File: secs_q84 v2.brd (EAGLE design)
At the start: 97.5 x 69.8 mm, 122 parts, among them IC1 MAX203ECWP, IC2 REF3440TIDBVR, IC3 ADP151AUJZ-3.3-R7, IC4 ADM3095EBRZ, IC5 MCZ33996EK, IC6 74HC125D, IC7 TIC12400DCPR, IC8 PIC18F57Q84-I_PT

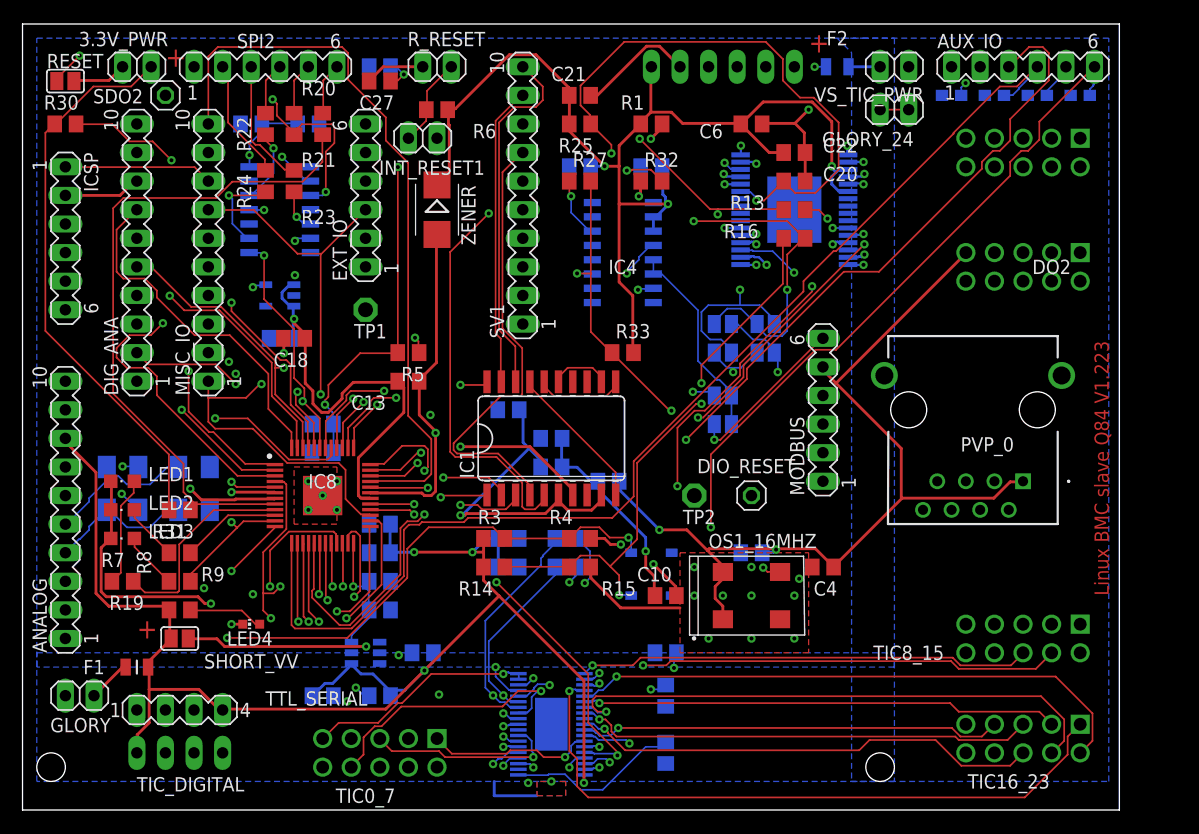
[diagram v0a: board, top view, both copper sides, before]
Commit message: add FM80 interface
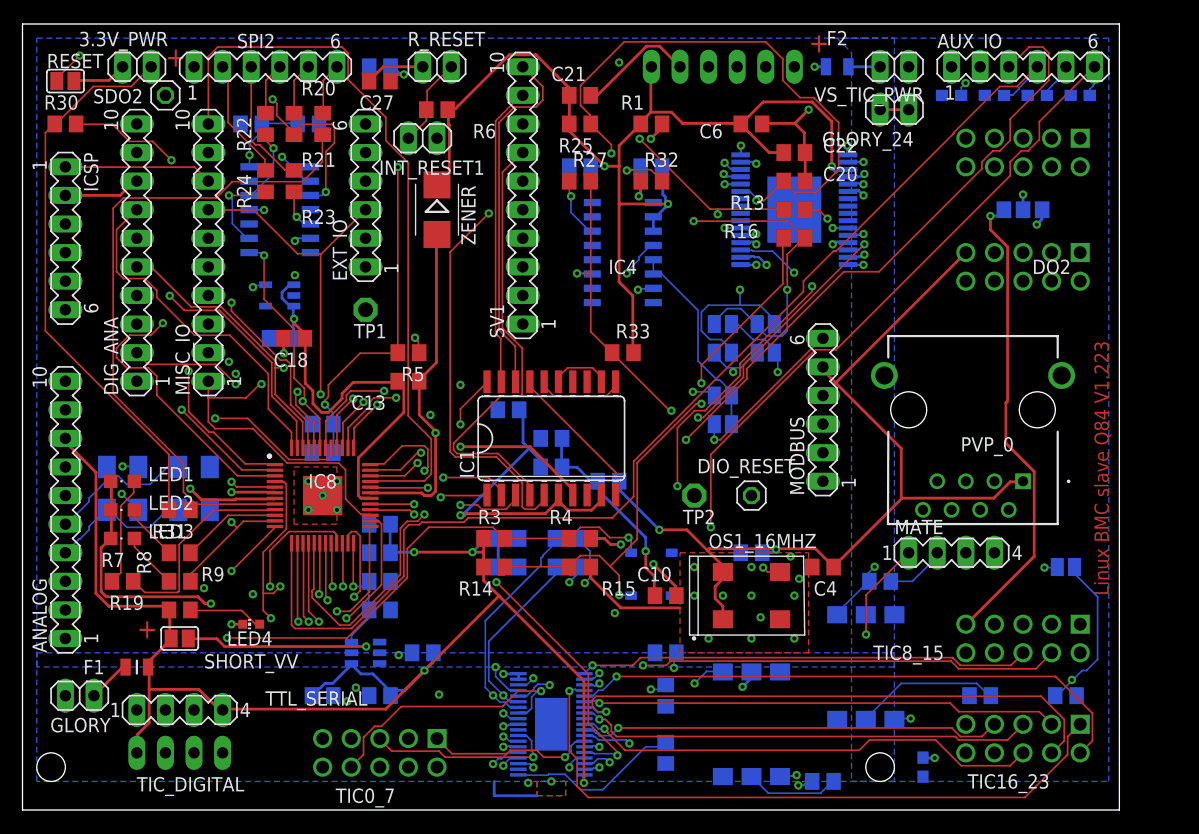
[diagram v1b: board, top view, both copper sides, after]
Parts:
- added C36: 0.1uf, rcl:C0603
- added FM_RS: FM_RS, jumper:SJ
- added JMP1: 0R-JUMPA, jump-0r-smd:A0R-JMP
- added MATE: MATE, con-lstb:MA04-1
- added OK1, OK2: 4N25SM, optocoupler:DIL6-SMD
- added R34, R35: 2.2k, rcl:R0805
- added R36: 1k, rcl:R0805
- added R37: 470, rcl:R0805
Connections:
- removed net VS_TIC_24V: C26.1, C27.1, F2.2, GLORY_24.1, GLORY_24.2, IC7.37, IC7.38, TIC0_7.9, TIC16_23.9, TIC8_15.9
- new net 0V: MATE.2, R34.2, R35.1
- new net FM80_24: MATE.1, OK2.5
- new net FM_RX: MATE.4, OK1.1
- new net FM_TX: MATE.3, OK2.4, R35.2
- new net MC_TIC_24V: C26.1, C27.1, F2.2, GLORY_24.1, GLORY_24.2, IC7.37, IC7.38, JMP1.3, TIC0_7.9, TIC16_23.9, TIC8_15.9
- new net N$13: FM_RS.1, IC1.20
- new net N$14: OK1.2, R34.1
- new net N$17: OK2.2, R37.1
- new net VPOWER: IC5.6, JMP1.2
- net PC_RX2: now also FM_RS.2, OK1.4, R36.2; no longer IC1.20
- net PC_TX2: now also OK2.1
- net VDD: now also C36.1, JMP1.1, OK1.5; no longer IC5.6
- net VSS: now also C36.2, R36.1, R37.2
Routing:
- net MC_TIC_24V: track 0.00 -> 194.9 mm, vias 0 -> 6
- net VS_TIC_24V: track 176.6 -> 0.00 mm, vias 4 -> 0
- net PC_RX2: track 61.4 -> 179.0 mm, vias 4 -> 6
- net N$13: track 0.00 -> 64.7 mm, vias 0 -> 3
- net VDD: track 478.3 -> 537.5 mm, vias 11 -> 14
- net PC_TX2: track 50.4 -> 104.8 mm, vias 3 -> 6
- net 0V: track 0.00 -> 42.1 mm, vias 0 -> 1
- net FM_RX: track 0.00 -> 38.8 mm, vias 0 -> 1
- net VPOWER: track 0.00 -> 23.4 mm, vias 0 -> 2
- net FM_TX: track 0.00 -> 14.5 mm, vias 0 -> 1
- net N$17: track 0.00 -> 12.9 mm
- net FM80_24: track 0.00 -> 10.6 mm, vias 0 -> 1
- net N$14: track 0.00 -> 8.36 mm

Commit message: up
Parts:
- R20, R21, R22, R23, R24: value 0ohm -> 56ohm
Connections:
- net PC_RX2: now also PVP_0.3
- net PC_TX2: now also PVP_0.8
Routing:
- net PC_RX2: track 179.0 -> 199.5 mm
- net PC_TX2: track 104.8 -> 123.3 mm
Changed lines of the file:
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@@
 <attribute name="VALUE" x="45.72" y="49.53" size="1.27" layer="28" rot="MR0"/>
 </element>
-<element name="R20" library="rcl" library_urn="urn:adsk.eagle:library:334" package="R0805" package3d_urn="urn:adsk.eagle:package:23553/2" value="0ohm" x="48.26" y="71.12" smashed="yes" rot="R270">
+<element name="R20" library="rcl" library_urn="urn:adsk.eagle:library:334" package="R0805" package3d_urn="urn:adsk.eagle:package:23553/2" value="56ohm" x="48.26" y="71.12" smashed="yes" rot="R270">
 <attribute name="NAME" x="46.355" y="73.66" size="1.27" layer="25"/>
 <attribute name="POPULARITY" value="85" x="48.26" y="71.12" size="1.778" layer="27" rot="R270" display="off"/>
@@
 <attribute name="VALUE" x="45.72" y="71.755" size="1.27" layer="27" rot="R270"/>
 </element>
-<element name="R21" library="rcl" library_urn="urn:adsk.eagle:library:334" package="R0805" package3d_urn="urn:adsk.eagle:package:23553/2" value="0ohm" x="45.72" y="71.12" smashed="yes" rot="R270">
+<element name="R21" library="rcl" library_urn="urn:adsk.eagle:library:334" package="R0805" package3d_urn="urn:adsk.eagle:package:23553/2" value="56ohm" x="45.72" y="71.12" smashed="yes" rot="R270">
 <attribute name="NAME" x="46.355" y="67.31" size="1.27" layer="25"/>
 <attribute name="POPULARITY" value="85" x="45.72" y="71.12" size="1.778" layer="27" rot="R270" display="off"/>
@@
 <attribute name="VALUE" x="43.18" y="71.755" size="1.27" layer="27" rot="R270"/>
 </element>
-<element name="R22" library="rcl" library_urn="urn:adsk.eagle:library:334" package="R0805" package3d_urn="urn:adsk.eagle:package:23553/2" value="0ohm" x="43.18" y="71.12" smashed="yes" rot="R270">
+<element name="R22" library="rcl" library_urn="urn:adsk.eagle:library:334" package="R0805" package3d_urn="urn:adsk.eagle:package:23553/2" value="56ohm" x="43.18" y="71.12" smashed="yes" rot="R270">
 <attribute name="NAME" x="40.64" y="71.755" size="1.27" layer="25" rot="R270"/>
 <attribute name="POPULARITY" value="85" x="43.18" y="71.12" size="1.778" layer="27" rot="R270" display="off"/>
@@
 <attribute name="VALUE" x="40.64" y="71.755" size="1.27" layer="27" rot="R270"/>
 </element>
-<element name="R23" library="rcl" library_urn="urn:adsk.eagle:library:334" package="R0805" package3d_urn="urn:adsk.eagle:package:23553/2" value="0ohm" x="45.72" y="66.04" smashed="yes" rot="R270">
+<element name="R23" library="rcl" library_urn="urn:adsk.eagle:library:334" package="R0805" package3d_urn="urn:adsk.eagle:package:23553/2" value="56ohm" x="45.72" y="66.04" smashed="yes" rot="R270">
 <attribute name="NAME" x="46.355" y="62.23" size="1.27" layer="25"/>
 <attribute name="POPULARITY" value="85" x="45.72" y="66.04" size="1.778" layer="27" rot="R270" display="off"/>
@@
 <attribute name="VALUE" x="43.18" y="66.675" size="1.27" layer="27" rot="R270"/>
 </element>
-<element name="R24" library="rcl" library_urn="urn:adsk.eagle:library:334" package="R0805" package3d_urn="urn:adsk.eagle:package:23553/2" value="0ohm" x="43.18" y="66.04" smashed="yes" rot="R270">
+<element name="R24" library="rcl" library_urn="urn:adsk.eagle:library:334" package="R0805" package3d_urn="urn:adsk.eagle:package:23553/2" value="56ohm" x="43.18" y="66.04" smashed="yes" rot="R270">
 <attribute name="NAME" x="40.64" y="66.675" size="1.27" layer="25" rot="R270"/>
 <attribute name="POPULARITY" value="85" x="43.18" y="66.04" size="1.778" layer="27" rot="R270" display="off"/>
@@
 <via x="81.3054" y="21.4122" extent="1-16" drill="0.35"/>
 <via x="114.8334" y="21.717" extent="1-16" drill="0.35"/>
+<contactref element="PVP_0" pad="3"/>
+<wire x1="107.9754" y1="34.4424" x2="107.9754" y2="39.3192" width="0.1524" layer="2"/>
+<wire x1="114.4524" y1="27.9654" x2="107.9754" y2="34.4424" width="0.1524" layer="2"/>
+<wire x1="114.4524" y1="22.098" x2="114.4524" y2="27.9654" width="0.1524" layer="2"/>
+<wire x1="114.8334" y1="21.717" x2="114.4524" y2="22.098" width="0.1524" layer="2"/>
+<wire x1="107.9754" y1="39.3192" x2="107.95" y2="39.37" width="0.1524" layer="2"/>
 </signal>
 <signal name="SS2">
@@
 <via x="87.1728" y="27.2796" extent="1-16" drill="0.35"/>
 <via x="74.2188" y="27.6606" extent="1-16" drill="0.35"/>
+<contactref element="PVP_0" pad="8"/>
+<wire x1="100.5078" y1="36.8046" x2="101.5746" y2="36.8046" width="0.1524" layer="1"/>
+<wire x1="93.0402" y1="29.337" x2="100.5078" y2="36.8046" width="0.1524" layer="1"/>
+<wire x1="91.2114" y1="29.337" x2="93.0402" y2="29.337" width="0.1524" layer="1"/>
+<wire x1="90.0684" y1="28.194" x2="91.2114" y2="29.337" width="0.1524" layer="1"/>
+<wire x1="87.8586" y1="28.194" x2="90.0684" y2="28.194" width="0.1524" layer="1"/>
+<wire x1="87.1728" y1="27.5082" x2="87.8586" y2="28.194" width="0.1524" layer="1"/>
+<wire x1="87.1728" y1="27.2796" x2="87.1728" y2="27.5082" width="0.1524" layer="1"/>
+<wire x1="101.5746" y1="36.8046" x2="101.6" y2="36.83" width="0.1524" layer="1"/>
 </signal>
 <signal name="ANA4">

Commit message: up
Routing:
- net VSS: track 109.6 -> 111.2 mm, vias 23 -> 24
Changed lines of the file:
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@@
 <param name="RoutingGrid" value="3mil"/>
 <param name="AutoGrid" value="1"/>
-<param name="Efforts" value="1"/>
+<param name="Efforts" value="0"/>
 <param name="TopRouterVariant" value="1"/>
 <param name="tpViaShape" value="round"/>
@@
 <vertex x="80.01" y="24.13"/>
 </polygon>
-<polygon width="0.1524" layer="1">
-<vertex x="67.31" y="11.43"/>
-<vertex x="69.85" y="11.43"/>
-<vertex x="69.85" y="12.7"/>
-<vertex x="67.31" y="12.7"/>
-</polygon>
-<polygon width="0.1524" layer="16">
-<vertex x="67.31" y="12.7"/>
-<vertex x="67.31" y="11.43"/>
-<vertex x="69.85" y="11.43"/>
-<vertex x="69.85" y="12.7"/>
-</polygon>
-<via x="68.58" y="12.7" extent="1-16" drill="0.35" locked="yes"/>
 <contactref element="C29" pad="2"/>
 <via x="82.55" y="25.4" extent="1-16" drill="0.35" locked="yes"/>
@@
 <via x="76.3524" y="64.6938" extent="1-16" drill="0.35"/>
 <via x="58.293" y="43.6626" extent="1-16" drill="0.35"/>
-<wire x1="67.31" y1="11.43" x2="63.5" y2="11.43" width="0.254" layer="16"/>
-<wire x1="63.5" y1="11.43" x2="63.5" y2="12.7" width="0.254" layer="16"/>
 <wire x1="80.01" y1="28.1178" x2="74.7522" y2="28.1178" width="0.254" layer="1"/>
 <contactref element="C35" pad="2"/>
@@
 <contactref element="R36" pad="1"/>
 <contactref element="C36" pad="2"/>
+<via x="64.77" y="25.4" extent="1-16" drill="0.35" locked="yes"/>
+<via x="60.96" y="20.32" extent="1-16" drill="0.35" locked="yes"/>
+<wire x1="64.77" y1="25.4" x2="60.96" y2="21.59" width="0.254" layer="1" locked="yes"/>
+<wire x1="60.96" y1="21.59" x2="60.96" y2="20.32" width="0.254" layer="1" locked="yes"/>
 </signal>
 <signal name="CPU_CLK">

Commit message: up
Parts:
- moved GLORY_24 2.54 mm to (96.5, 72.4)
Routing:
- net MC_TIC_24V: track 194.9 -> 196.4 mm
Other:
- board text added: "Linux BMC slave Q84 V1.308"
- board text removed: "Linux BMC slave Q84 V1.223"

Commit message: update board to 1.308
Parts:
- added LED5: FM80 POWER, led:CHIP-LED0603
- added R38: 10k, rcl:R0805
- renumbered JMP1 to VDD-TIC
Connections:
- new net N$15: LED5.A, R38.2
- net 0V: now also LED5.C
- net FM80_24: now also R38.1
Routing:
- net FM80_24: track 10.6 -> 42.2 mm, vias 1 -> 2
- net 0V: track 42.1 -> 69.2 mm
- net N$15: track 0.00 -> 3.63 mm, vias 0 -> 1
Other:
- board size 97.5 x 69.8 mm -> 102.5 x 69.8 mm
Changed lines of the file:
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@@
 <layers>
 <layer number="1" name="Top" color="4" fill="1" visible="yes" active="yes"/>
-<layer number="2" name="Route2" color="16" fill="1" visible="yes" active="yes"/>
+<layer number="2" name="Route2" color="16" fill="1" visible="no" active="yes"/>
 <layer number="3" name="Route3" color="17" fill="1" visible="no" active="no"/>
 <layer number="4" name="Route4" color="18" fill="1" visible="no" active="no"/>
@@
 <layer number="13" name="Route13" color="21" fill="1" visible="no" active="no"/>
 <layer number="14" name="Route14" color="22" fill="1" visible="no" active="no"/>
-<layer number="15" name="Route15" color="23" fill="1" visible="yes" active="yes"/>
+<layer number="15" name="Route15" color="23" fill="1" visible="no" active="yes"/>
 <layer number="16" name="Bottom" color="1" fill="1" visible="yes" active="yes"/>
 <layer number="17" name="Pads" color="2" fill="1" visible="yes" active="yes"/>
@@
 <layer number="19" name="Unrouted" color="6" fill="1" visible="yes" active="yes"/>
 <layer number="20" name="Dimension" color="24" fill="1" visible="yes" active="yes"/>
-<layer number="21" name="tPlace" color="7" fill="1" visible="yes" active="yes"/>
+<layer number="21" name="tPlace" color="7" fill="1" visible="no" active="yes"/>
 <layer number="22" name="bPlace" color="7" fill="1" visible="yes" active="yes"/>
-<layer number="23" name="tOrigins" color="15" fill="1" visible="yes" active="yes"/>
+<layer number="23" name="tOrigins" color="15" fill="1" visible="no" active="yes"/>
 <layer number="24" name="bOrigins" color="15" fill="1" visible="yes" active="yes"/>
-<layer number="25" name="tNames" color="7" fill="1" visible="yes" active="yes"/>
+<layer number="25" name="tNames" color="7" fill="1" visible="no" active="yes"/>
 <layer number="26" name="bNames" color="7" fill="1" visible="yes" active="yes"/>
 <layer number="27" name="tValues" color="7" fill="1" visible="no" active="yes"/>
@@
 <layer number="37" name="tTest" color="7" fill="1" visible="no" active="yes"/>
 <layer number="38" name="bTest" color="7" fill="1" visible="no" active="yes"/>
-<layer number="39" name="tKeepout" color="4" fill="11" visible="yes" active="yes"/>
+<layer number="39" name="tKeepout" color="4" fill="11" visible="no" active="yes"/>
 <layer number="40" name="bKeepout" color="1" fill="11" visible="yes" active="yes"/>
-<layer number="41" name="tRestrict" color="4" fill="10" visible="yes" active="yes"/>
+<layer number="41" name="tRestrict" color="4" fill="10" visible="no" active="yes"/>
 <layer number="42" name="bRestrict" color="1" fill="10" visible="yes" active="yes"/>
 <layer number="43" name="vRestrict" color="2" fill="10" visible="no" active="yes"/>
@@
 <layer number="48" name="Document" color="7" fill="1" visible="no" active="yes"/>
 <layer number="49" name="Reference" color="7" fill="1" visible="no" active="yes"/>
-<layer number="51" name="tDocu" color="7" fill="1" visible="yes" active="yes"/>
+<layer number="51" name="tDocu" color="7" fill="1" visible="no" active="yes"/>
 <layer number="52" name="bDocu" color="7" fill="1" visible="yes" active="yes"/>
 <layer number="88" name="SimResults" color="9" fill="1" visible="no" active="no"/>
@@
 <board>
 <plain>
-<wire x1="21.59" y1="10.16" x2="119.05" y2="10.16" width="0" layer="20"/>
-<wire x1="119.05" y1="10.16" x2="119.05" y2="80" width="0" layer="20"/>
-<wire x1="119.05" y1="80" x2="21.59" y2="80" width="0" layer="20"/>
+<wire x1="21.59" y1="10.16" x2="124.13" y2="10.16" width="0" layer="20"/>
+<wire x1="124.13" y1="10.16" x2="124.13" y2="80" width="0" layer="20"/>
+<wire x1="124.13" y1="80" x2="21.59" y2="80" width="0" layer="20"/>
 <wire x1="21.59" y1="80" x2="21.59" y2="10.16" width="0" layer="20"/>
-<text x="118.11" y="29.21" size="1.27" layer="1" font="vector" ratio="15" distance="70" rot="R90">Linux BMC slave Q84 V1.308</text>
+<text x="123.19" y="29.21" size="1.27" layer="1" font="vector" ratio="15" distance="70" rot="R90">Linux BMC slave Q84 V1.308</text>
 <polygon width="0.1524" layer="43">
 <vertex x="40.64" y="45.72"/>
@@
 <attribute name="VALUE" x="104.775" y="71.755" size="1.27" layer="28" rot="MR0"/>
 </element>
-<element name="JMP1" library="jump-0r-smd" library_urn="urn:adsk.eagle:library:251" package="A0R-JMP" package3d_urn="urn:adsk.eagle:package:15385/1" value="0R-JUMPA" x="110.49" y="63.5" smashed="yes" rot="MR90">
-<attribute name="NAME" x="113.206" y="64.008" size="1.27" layer="26" rot="MR180"/>
+<element name="VDD-TIC" library="jump-0r-smd" library_urn="urn:adsk.eagle:library:251" package="A0R-JMP" package3d_urn="urn:adsk.eagle:package:15385/1" value="0R-JUMPA" x="110.49" y="63.5" smashed="yes" rot="MR90">
+<attribute name="NAME" x="113.792" y="53.516" size="1.27" layer="26" rot="MR0"/>
 <attribute name="POPULARITY" value="3" x="110.49" y="63.5" size="1.778" layer="28" rot="MR90" display="off"/>
 <attribute name="VALUE" x="106.504" y="62.738" size="1.27" layer="28" rot="MR90"/>
@@
 <attribute name="VALUE" x="114.7001" y="31.75" size="0.02" layer="28" rot="MR180"/>
 </element>
+<element name="LED5" library="led" library_urn="urn:adsk.eagle:library:259" package="CHIP-LED0603" package3d_urn="urn:adsk.eagle:package:15819/3" value="FM80 POWER" x="121.92" y="20.32" smashed="yes">
+<attribute name="NAME" x="122.555" y="22.225" size="1.27" layer="25" rot="R90"/>
+<attribute name="POPULARITY" value="26" x="121.92" y="20.32" size="1.778" layer="27" display="off"/>
+<attribute name="VALUE" x="123.825" y="19.685" size="1.27" layer="27" rot="R90"/>
+</element>
+<element name="R38" library="rcl" library_urn="urn:adsk.eagle:library:334" package="R0805" package3d_urn="urn:adsk.eagle:package:23553/2" value="10k" x="121.92" y="15.24" smashed="yes" rot="MR90">
+<attribute name="NAME" x="119.38" y="12.065" size="1.27" layer="26" rot="MR90"/>
+<attribute name="POPULARITY" value="85" x="121.92" y="15.24" size="1.778" layer="28" rot="MR90" display="off"/>
+<attribute name="SPICEPREFIX" value="R" x="121.92" y="15.24" size="1.778" layer="28" rot="MR90" display="off"/>
+<attribute name="VALUE" x="119.38" y="14.605" size="1.27" layer="28" rot="MR90"/>
+</element>
 </elements>
 <signals>
@@
 <via x="73.3044" y="67.3608" extent="1-16" drill="0.35"/>
 <via x="78.9432" y="64.008" extent="1-16" drill="0.35"/>
-<contactref element="JMP1" pad="1"/>
+<contactref element="VDD-TIC" pad="1"/>
 <contactref element="IC5" pad="3"/>
 <wire x1="112.1664" y1="62.6364" x2="112.1664" y2="63.4746" width="0.254" layer="16"/>
@@
 <vertex x="118.11" y="12.7"/>
 <vertex x="118.11" y="78.74"/>
-<vertex x="96.52" y="78.74"/>
 <vertex x="93.98" y="78.74"/>
 <vertex x="95.25" y="77.47"/>
@@
 <contactref element="GLORY_24" pad="2"/>
 <contactref element="GLORY_24" pad="1"/>
-<contactref element="JMP1" pad="3"/>
+<contactref element="VDD-TIC" pad="3"/>
 <via x="107.5944" y="62.9412" extent="1-16" drill="0.35"/>
 <wire x1="108.204" y1="62.9412" x2="107.5944" y2="62.9412" width="0.254" layer="16"/>
@@
 </signal>
 <signal name="VPOWER" class="1">
-<contactref element="JMP1" pad="2"/>
+<contactref element="VDD-TIC" pad="2"/>
 <contactref element="IC5" pad="6"/>
 <wire x1="110.49" y1="64.8462" x2="110.49" y2="63.5" width="0.254" layer="16"/>
@@
 <wire x1="102.87" y1="32.9946" x2="102.87" y2="33.02" width="0.1524" layer="16"/>
 <via x="90.5256" y="12.3444" extent="1-16" drill="0.35"/>
+<contactref element="LED5" pad="C"/>
+<wire x1="120.1674" y1="21.1074" x2="121.92" y2="21.1074" width="0.1524" layer="1"/>
+<wire x1="115.7478" y1="25.527" x2="120.1674" y2="21.1074" width="0.1524" layer="1"/>
+<wire x1="105.0036" y1="25.527" x2="115.7478" y2="25.527" width="0.1524" layer="1"/>
+<wire x1="102.87" y1="27.6606" x2="105.0036" y2="25.527" width="0.1524" layer="1"/>
+<wire x1="102.87" y1="33.02" x2="102.87" y2="27.6606" width="0.1524" layer="1"/>
+<wire x1="121.92" y1="21.1074" x2="121.92" y2="21.07" width="0.1524" layer="1"/>
 </signal>
 <signal name="FM80_24">
@@
 <wire x1="100.2792" y1="32.9946" x2="100.33" y2="33.02" width="0.1524" layer="1"/>
 <via x="96.5454" y="25.7556" extent="1-16" drill="0.35"/>
+<contactref element="R38" pad="1"/>
+<wire x1="120.6246" y1="15.621" x2="121.92" y2="14.3256" width="0.1524" layer="16"/>
+<wire x1="120.6246" y1="17.526" x2="120.6246" y2="15.621" width="0.1524" layer="1"/>
+<wire x1="114.1476" y1="24.003" x2="120.6246" y2="17.526" width="0.1524" layer="1"/>
+<wire x1="114.1476" y1="24.6126" x2="114.1476" y2="24.003" width="0.1524" layer="1"/>
+<wire x1="113.538" y1="25.2222" x2="114.1476" y2="24.6126" width="0.1524" layer="1"/>
+<wire x1="97.0788" y1="25.2222" x2="113.538" y2="25.2222" width="0.1524" layer="1"/>
+<wire x1="96.5454" y1="25.7556" x2="97.0788" y2="25.2222" width="0.1524" layer="1"/>
+<wire x1="121.92" y1="14.3256" x2="121.92" y2="14.29" width="0.1524" layer="16"/>
+<via x="120.6246" y="15.621" extent="1-16" drill="0.35"/>
 </signal>
 <signal name="N$13">
@@
 <via x="60.5028" y="44.4246" extent="1-16" drill="0.35"/>
 </signal>
+<signal name="N$15">
+<contactref element="LED5" pad="A"/>
+<contactref element="R38" pad="2"/>
+<wire x1="121.92" y1="18.669" x2="121.92" y2="19.57" width="0.1524" layer="1"/>
+<wire x1="122.0724" y1="18.5166" x2="121.92" y2="18.669" width="0.1524" layer="1"/>
+<wire x1="122.0724" y1="18.288" x2="122.0724" y2="18.5166" width="0.1524" layer="16"/>
+<wire x1="122.2248" y1="18.1356" x2="122.0724" y2="18.288" width="0.1524" layer="16"/>
+<wire x1="122.2248" y1="16.5354" x2="122.2248" y2="18.1356" width="0.1524" layer="16"/>
+<wire x1="121.92" y1="16.2306" x2="122.2248" y2="16.5354" width="0.1524" layer="16"/>
+<wire x1="121.92" y1="16.2306" x2="121.92" y2="16.19" width="0.1524" layer="16"/>
+<via x="122.0724" y="18.5166" extent="1-16" drill="0.35"/>
+</signal>
 </signals>
